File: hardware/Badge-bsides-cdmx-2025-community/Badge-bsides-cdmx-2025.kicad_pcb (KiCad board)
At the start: 2 copper layers, 49.9 x 109.8 mm, 39 parts, among them J1 SWDIO, J3 ADDON, J4 Conn_01x04_Pin, J5 I2C, J6 Conn_01x04_Pin, SW10 SW_Push, SW11 ON, SW2 RESET, SW7 SW_Push, SW8 SW_Push, SW9 SW_Push, U1 PY32F030F28U6TR

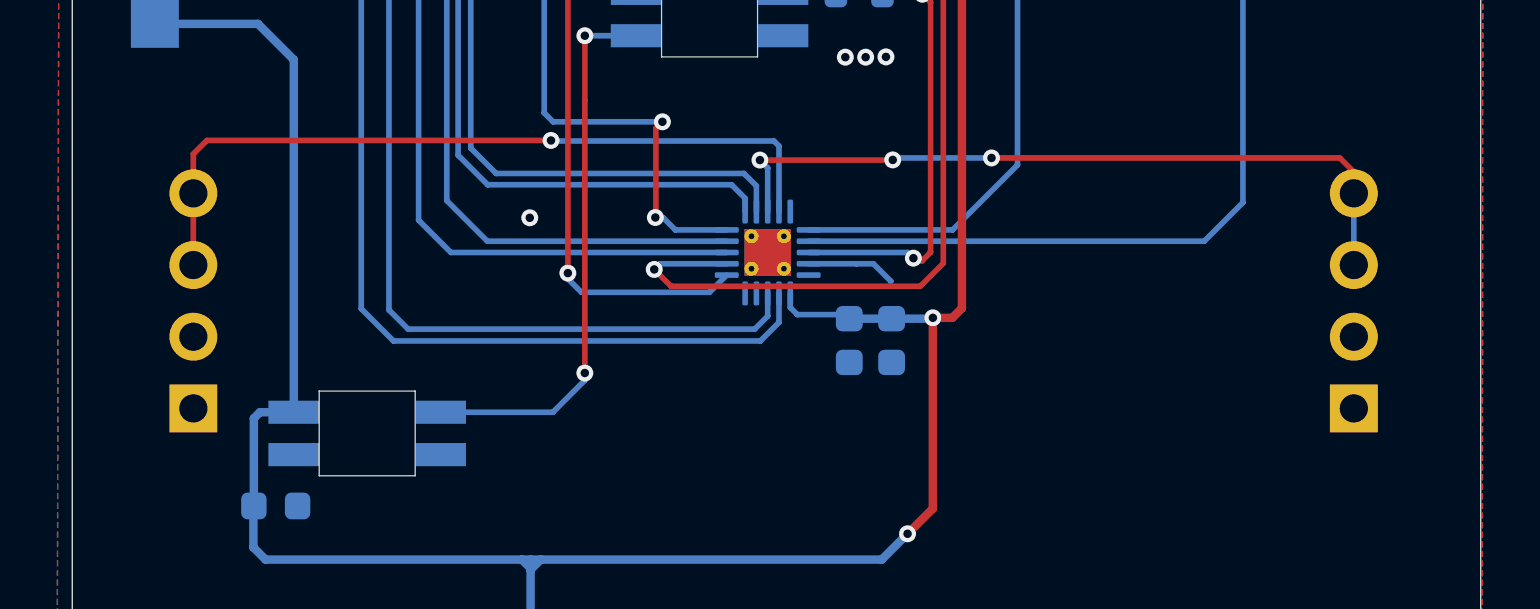
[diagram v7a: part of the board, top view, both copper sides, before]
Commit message: fix(Hw):Connectors_moved
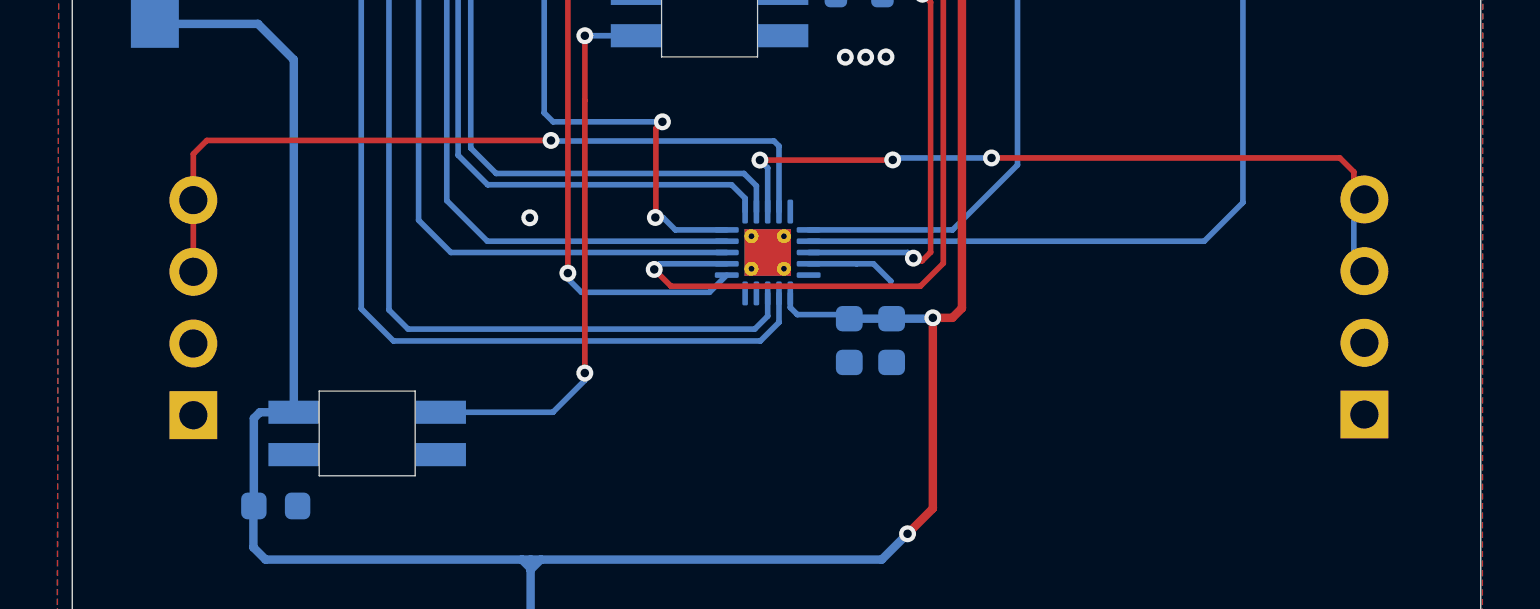
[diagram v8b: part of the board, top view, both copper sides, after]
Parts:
- moved J4 0.43 mm to (80.2, 83.1)
- moved J6 0.24 mm to (38.7, 83.1)
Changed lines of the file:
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@@
 	(footprint "Connector_PinSocket_2.54mm:PinSocket_1x04_P2.54mm_Horizontal"
 		(layer "B.Cu")
-		(at 38.691333 82.864333)
+		(at 38.691333 83.104333)
 		(descr "Through hole angled socket strip, 1x04, 2.54mm pitch, 8.51mm socket length, single row (from Kicad 4.0.7), script generated")
 		(tags "Through hole angled socket strip THT 1x04 2.54mm single row")
@@
 	(footprint "Connector_PinHeader_2.54mm:PinHeader_1x04_P2.54mm_Horizontal"
 		(layer "B.Cu")
-		(at 79.806333 82.864333)
+		(at 80.18 83.08)
 		(descr "Through hole angled pin header, 1x04, 2.54mm pitch, 6mm pin length, single row")
 		(tags "Through hole angled pin header THT 1x04 2.54mm single row")
